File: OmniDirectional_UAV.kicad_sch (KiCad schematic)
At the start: 45 parts

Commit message: add circuits
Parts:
- added D?: LED, symbol Device:LED
- added J?: motor, symbol Connector_Generic:Conn_01x02
- added R?: 20k, symbol Device:R_Small
- added R?: 1k, symbol Device:R_Small
- added R? (x2): 10k, symbol Device:R_Small
- added U?: DRV8835, symbol My_Device:DRV8835
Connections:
- net +3.3V: now also U?.12 (VCC)
- net +BATT: now also R?.1, U?.1 (VM)
- net GND: now also U?.63 (VSS), D?.1 (K), R?.2, R?.2, U?.11 (MODE), U?.13 (GND_TP), U?.6 (GND)
- net USART1_RX: now reaches J?.1 (Pin_1)
- net USART1_RX: now also U?.43 (PA10)
- net USART1_TX: now reaches J?.2 (Pin_2)
- net USART1_TX: now also U?.42 (PA9)
- net TIM9_CH1_BUZZER: now reaches Q?.2 (G), R?.1
- net TIM9_CH1_BUZZER: now also U?.16 (PA2)
- net SPI_CS: now reaches U?.22 (nCS)
- net SPI_CS: now also U?.20 (PA4)
- net SPI_SCK: now reaches U?.23 (SCL/SCLK)
- net SPI_SCK: now also U?.21 (PA5)
- net SPI_MOSI: now reaches U?.24 (SDA/SDI)
- net SPI_MOSI: now also U?.23 (PA7)
- net SPI_MISO: now reaches U?.9 (ADO/SDO)
- net SPI_MISO: now also U?.22 (PA6)
- net LED3: now reaches R?.1
- net LED3: now also U?.34 (PB13)
- net TIM2_CH1_MOTOR1_IN1: now reaches U?.10 (AIN1), U?.8 (BIN1)
- net TIM2_CH1_MOTOR1_IN1: now also U?.50 (PA15)
- net TIM2_CH2_MOTOR1_IN2: now reaches U?.7 (BIN2), U?.9 (AIN2)
- net TIM2_CH2_MOTOR1_IN2: now also U?.55 (PB3)
- net LED4: now reaches R?.1
- net LED4: now also U?.33 (PB12)
- net BUTTON: now reaches C?.1, R?.2, SW?.4 (D)
- net BUTTON: now also U?.28 (PB2)
- net NRST: now reaches C?.1, SW?.2 (D)
- net NRST: now also J?.4 (Pin_4), U?.7 (NRST)
- net SWCLK: now reaches J?.1 (Pin_1)
- net SWCLK: now also U?.49 (PA14)
- net SWDIO: now reaches J?.2 (Pin_2)
- net SWDIO: now also U?.46 (PA13)
- net LED2: now reaches R?.1
- net LED2: now also U?.35 (PB14)
- net TIM5_CH1_MOTOR7_IN1: now reaches U?.14 (PA0_WKUP)
- net TIM5_CH2_MOTOR7_IN2: now reaches U?.15 (PA1)
- net TIM2_CH4_MOTOR2_IN2: now reaches U?.17 (PA3)
- net TIM2_CH4_MOTOR2_IN2: now also U?.7 (BIN2), U?.9 (AIN2)
- net TIM3_CH3_MOTOR4_IN1: now reaches U?.26 (PB0)
- net ADC_BAT: now reaches U?.27 (PB1)
- net ADC_BAT: now also R?.1, R?.2
- net TIM2_CH3_MOTOR2_IN1: now reaches U?.29 (PB10)
- net TIM2_CH3_MOTOR2_IN1: now also U?.10 (AIN1), U?.8 (BIN1)
- net LED1: now reaches U?.36 (PB15)
- net LED1: now also R?.1
- net TIM8_CH1_MOTOR8_IN1: now reaches U?.37 (PC6)
- net TIM8_CH2_MOTOR8_IN2: now reaches U?.38 (PC7)
- net TIM3_CH4_MOTOR4_IN2: now reaches U?.40 (PC9)
- net TIM3_CH1_MOTOR3_IN1: now reaches U?.56 (PB4)
- net TIM3_CH2_MOTOR3_IN2: now reaches U?.57 (PB5)
- net TIM4_CH1_MOTOR5_IN1: now reaches U?.58 (PB6)
- net TIM4_CH2_MOTOR5_IN2: now reaches U?.59 (PB7)
- net BOOT0: now reaches U?.60 (BOOT0)
- net BOOT0: now also R?.1
- net TIM4_CH3_MOTOR6_IN1: now reaches U?.61 (PB8)
- net TIM4_CH4_MOTOR6_IN2: now reaches U?.62 (PB9)
- new net: D?.2 (A), R?.2
- new net: J?.1 (Pin_1), U?.2 (AOUT1), U?.4 (BOUT1)
- new net: J?.2 (Pin_2), U?.3 (AOUT2), U?.5 (BOUT2)
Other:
- moved on the sheet: C?, D?, J?, R?, SW?A, SW?B, U?

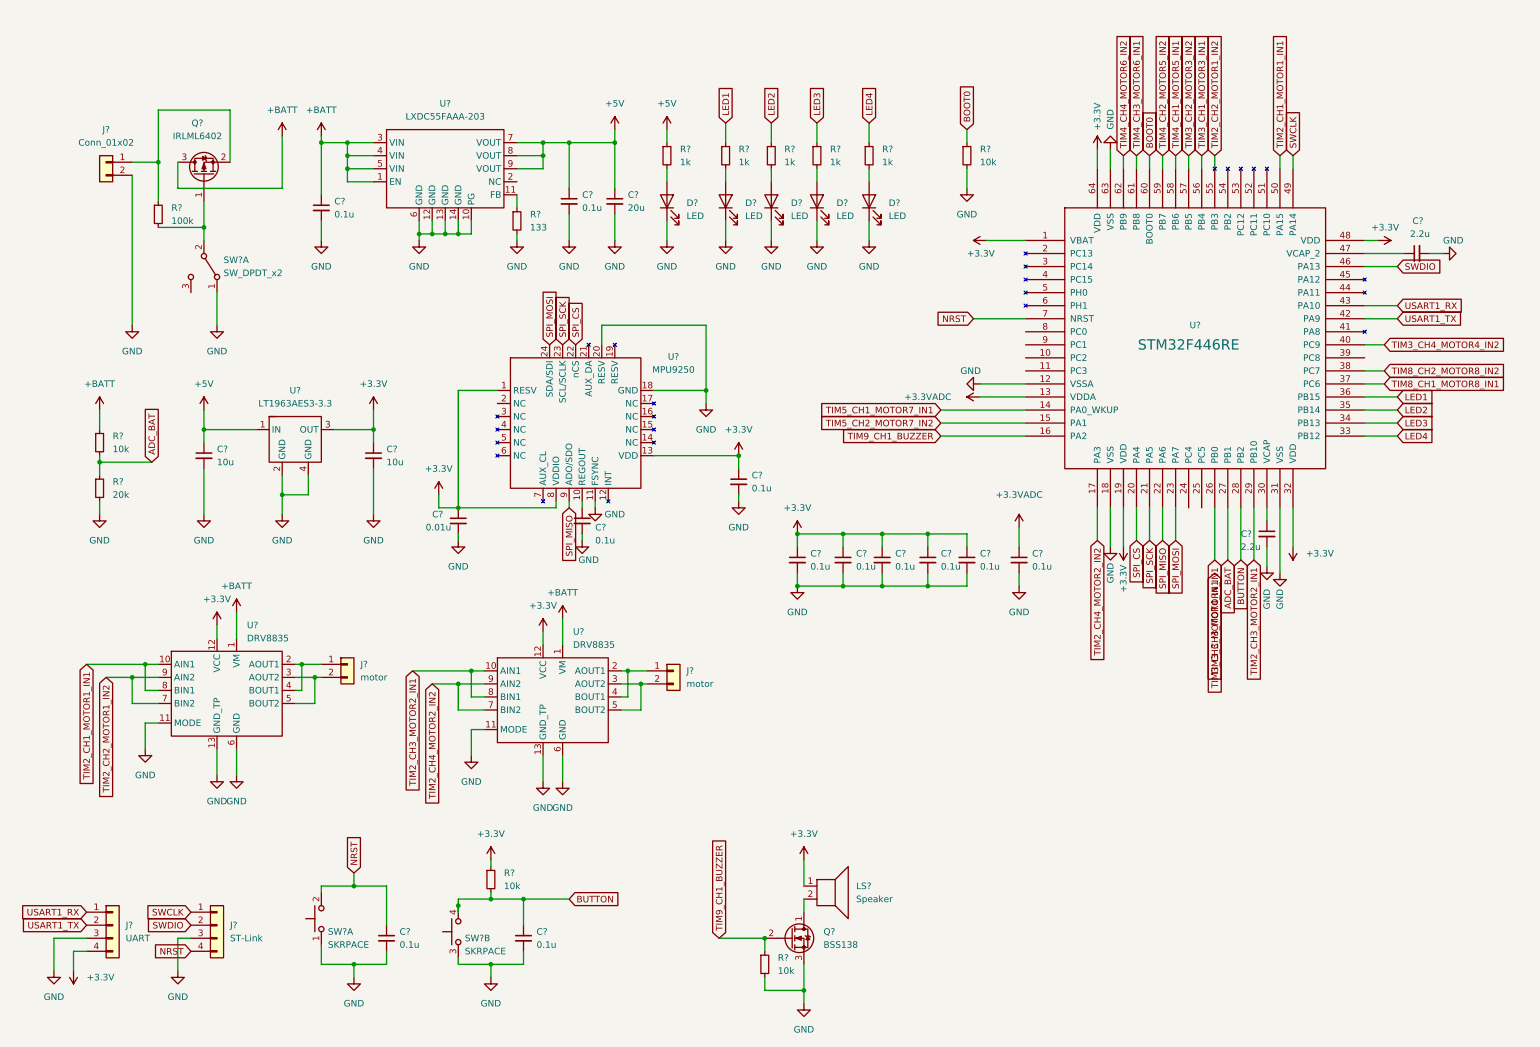
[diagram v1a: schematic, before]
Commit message: add hierarchical sheets
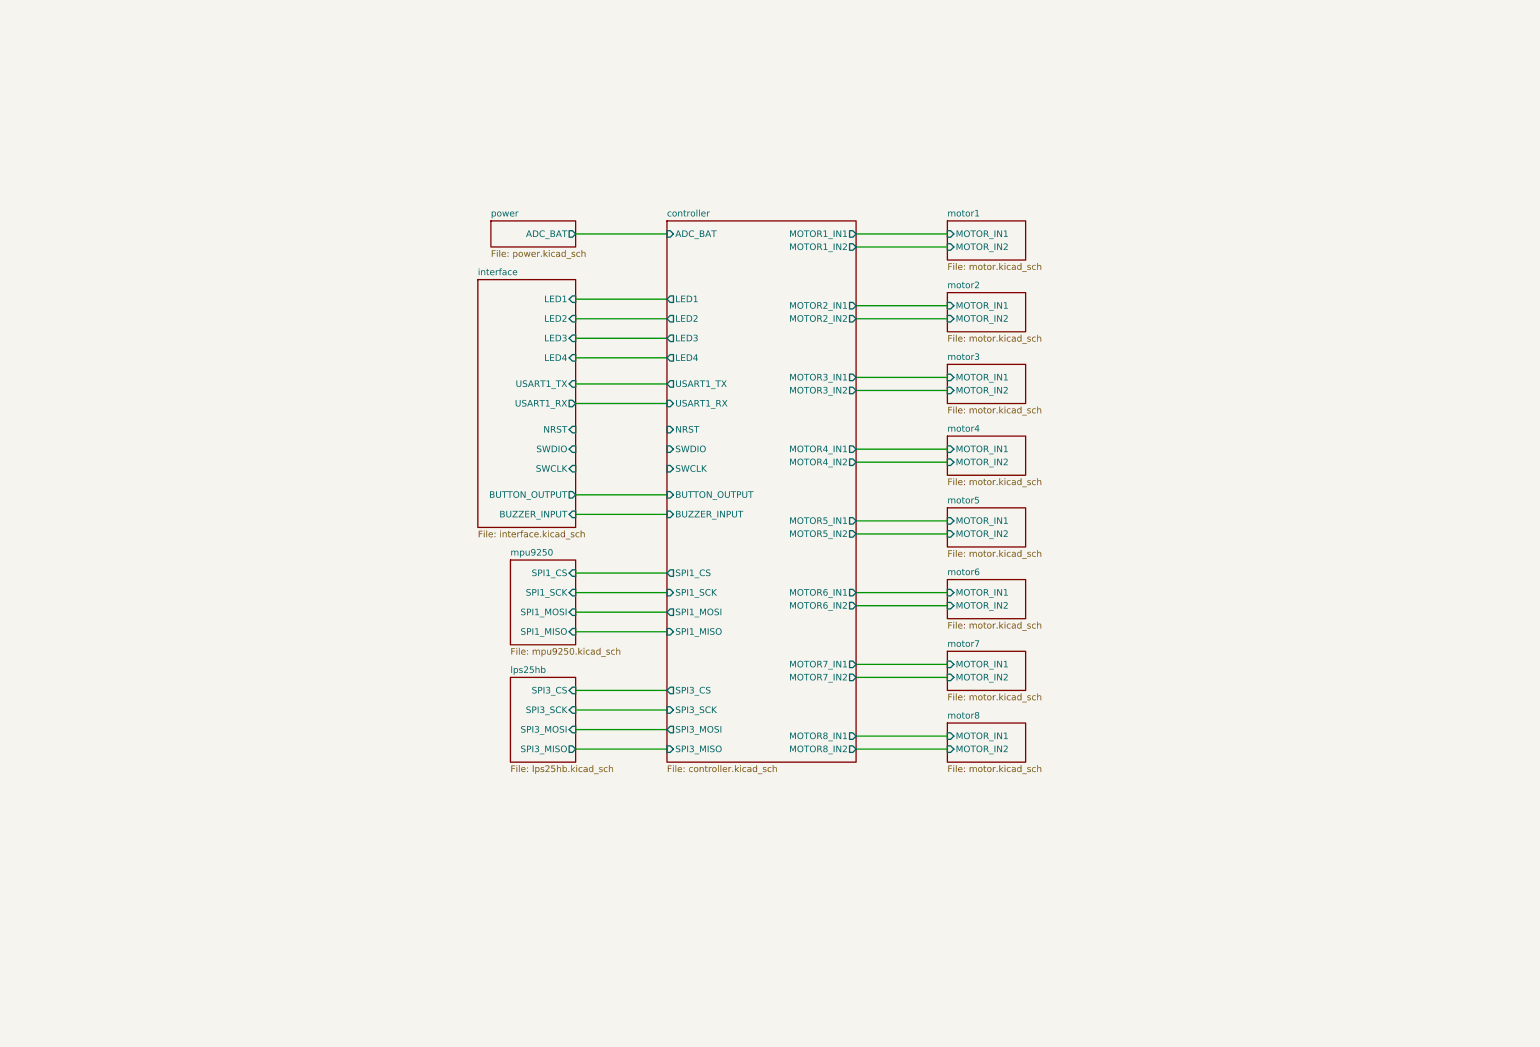
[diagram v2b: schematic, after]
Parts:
- removed C? (x12): 0.1u, symbol Device:C_Small
- removed C? (x2): 10u, symbol Device:C_Small
- removed C?: 0.01u, symbol Device:C_Small
- removed C? (x2): 2.2u, symbol Device:C_Small
- removed C?: 20u, symbol Device:C_Small
- removed D? (x5): LED, symbol Device:LED
- removed J?: UART, symbol Connector_Generic:Conn_01x04
- removed J? (x2): motor, symbol Connector_Generic:Conn_01x02
- removed J?: ST-Link, symbol Connector_Generic:Conn_01x04
- removed J?: Conn_01x02, symbol Connector_Generic:Conn_01x02
- removed LS?: Speaker, symbol Device:Speaker
- removed Q?: BSS138, symbol Device:Q_NMOS_DGS
- removed Q?: IRLML6402, Package_TO_SOT_SMD:SOT-23, symbol Transistor_FET:AO3401A
- removed R? (x5): 1k, symbol Device:R_Small
- removed R? (x4): 10k, symbol Device:R_Small
- removed R?: 20k, symbol Device:R_Small
- removed R?: 100k, symbol Device:R_Small
- removed R?: 133, symbol Device:R_Small
- removed SW? (x2): SKRPACE, symbol Switch:SW_Push_Dual_x2
- removed SW?: SW_DPDT_x2, symbol Switch:SW_DPDT_x2
- removed U?: MPU9250, symbol My_Device:MPU9250
- removed U? (x2): DRV8835, symbol My_Device:DRV8835
- removed U?: LT1963AES3-3.3, symbol My_Device:LT1963AES3-3.3
- removed U?: STM32F446RE, Package_QFP:LQFP-64_10x10mm_P0.5mm, symbol My_Device:STM32F446RE
- removed U?: LXDC55FAAA-203, symbol My_Device:LXDC55FAAA-203
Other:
- added sheet controller (controller.kicad_sch)
- added sheet interface (interface.kicad_sch)
- added sheet lps25hb (lps25hb.kicad_sch)
- added sheet motor1 (motor.kicad_sch)
- added sheet motor2 (motor.kicad_sch)
- added sheet motor3 (motor.kicad_sch)
- added sheet motor4 (motor.kicad_sch)
- added sheet motor5 (motor.kicad_sch)
- added sheet motor6 (motor.kicad_sch)
- added sheet motor7 (motor.kicad_sch)
- added sheet motor8 (motor.kicad_sch)
- added sheet mpu9250 (mpu9250.kicad_sch)
- added sheet power (power.kicad_sch)

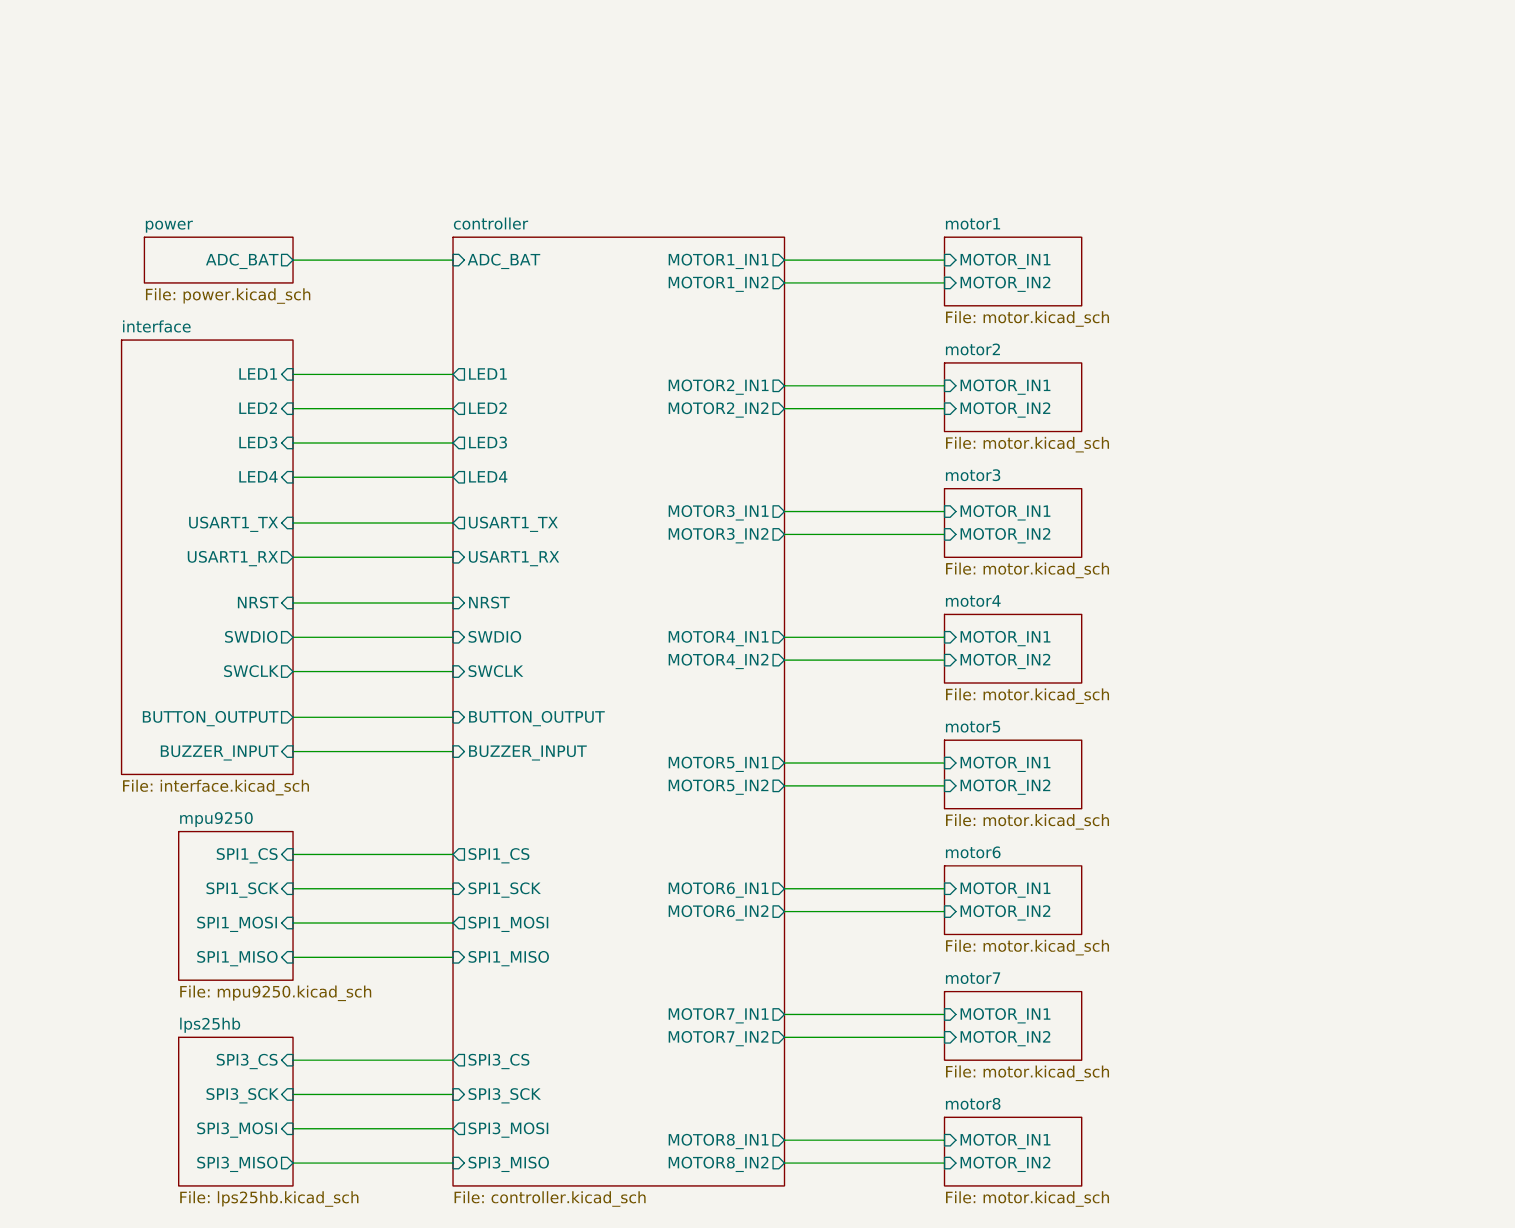
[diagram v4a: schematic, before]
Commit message: 部品配置完了
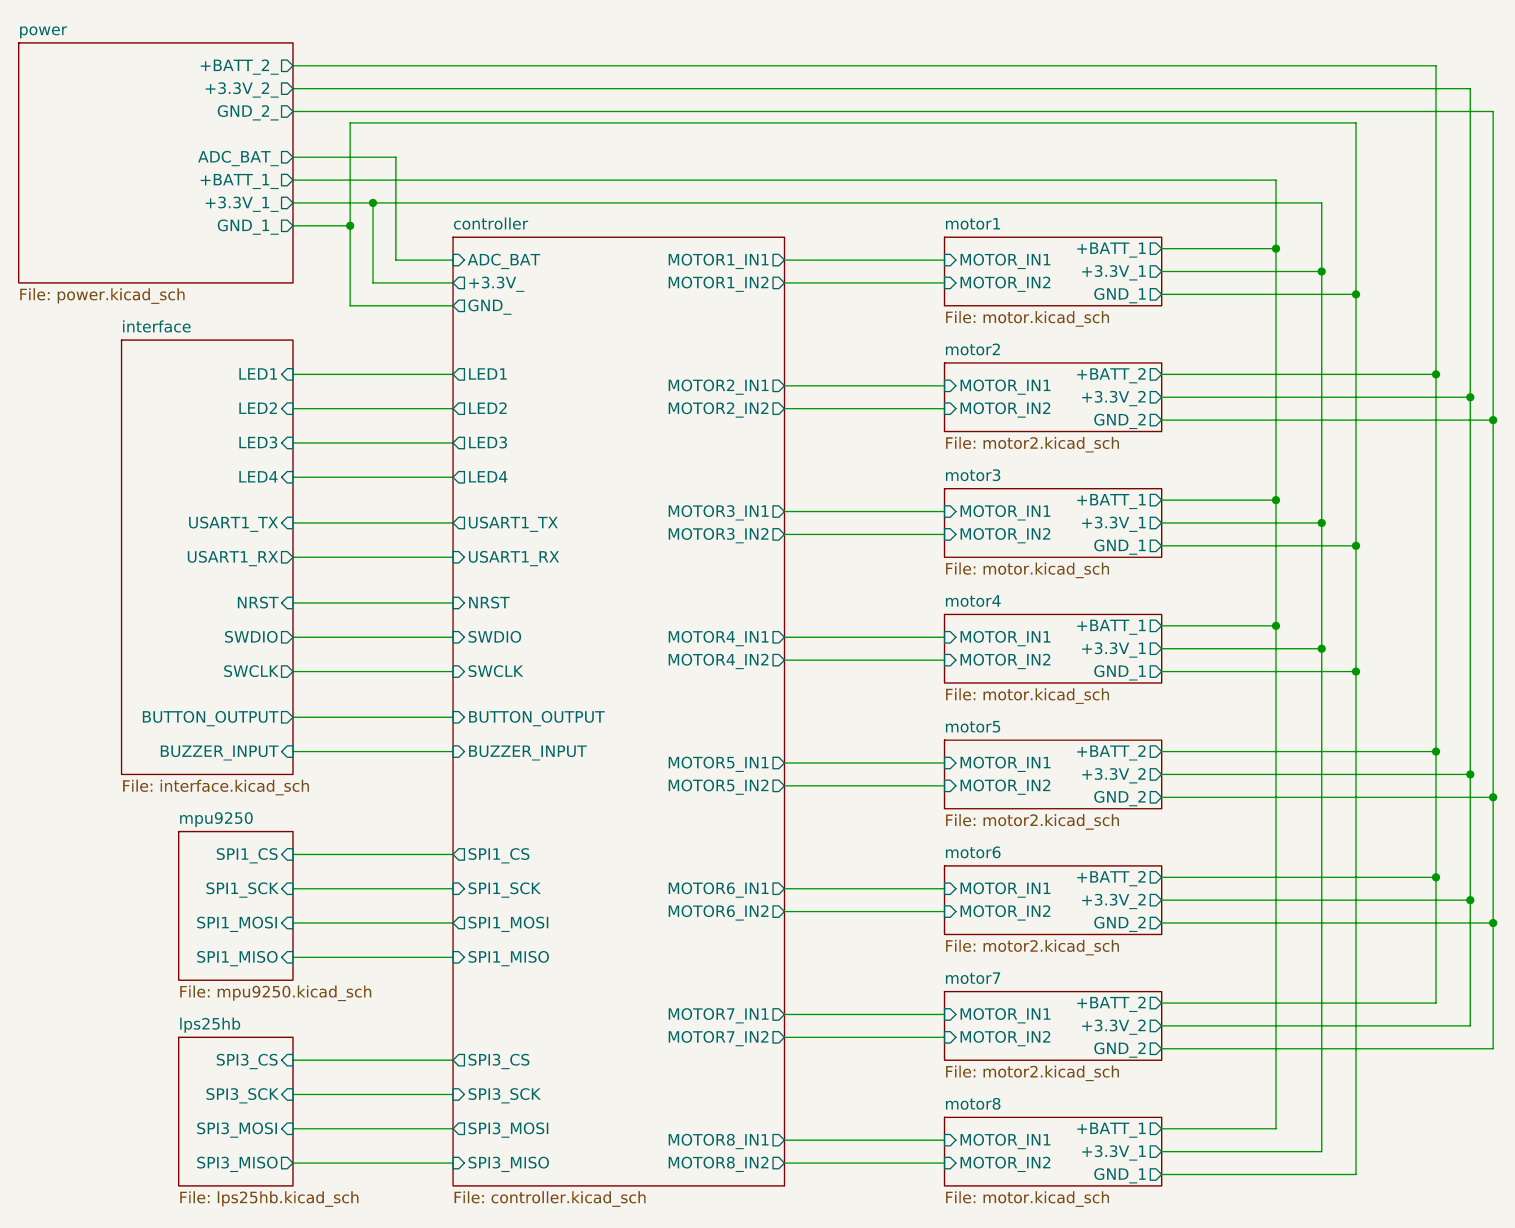
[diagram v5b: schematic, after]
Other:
- sheet controller ports: added +3.3V_, GND_; removed none
- sheet motor1 ports: added +3.3V_1, +BATT_1, GND_1; removed none
- sheet motor2: file motor.kicad_sch -> motor2.kicad_sch
- sheet motor2 ports: added +3.3V_2, +BATT_2, GND_2; removed none
- sheet motor3 ports: added +3.3V_1, +BATT_1, GND_1; removed none
- sheet motor4 ports: added +3.3V_1, +BATT_1, GND_1; removed none
- sheet motor5: file motor.kicad_sch -> motor2.kicad_sch
- sheet motor5 ports: added +3.3V_2, +BATT_2, GND_2; removed none
- sheet motor6: file motor.kicad_sch -> motor2.kicad_sch
- sheet motor6 ports: added +3.3V_2, +BATT_2, GND_2; removed none
- sheet motor7: file motor.kicad_sch -> motor2.kicad_sch
- sheet motor7 ports: added +3.3V_2, +BATT_2, GND_2; removed none
- sheet motor8 ports: added +3.3V_1, +BATT_1, GND_1; removed none
- sheet power ports: added +3.3V_1_, +3.3V_2_, +BATT_1_, +BATT_2_, ADC_BAT_, GND_1_, GND_2_; removed ADC_BAT
